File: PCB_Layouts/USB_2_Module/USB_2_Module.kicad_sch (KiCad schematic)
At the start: 3 parts, among them J1 USB_A, J2 Conn_01x10_Socket, J3 Conn_01x10_Socket

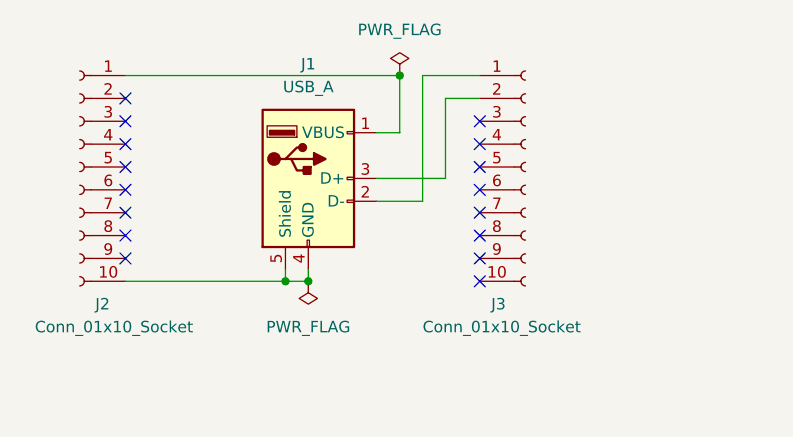
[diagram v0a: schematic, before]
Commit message: Adding USB 2 module and  quote
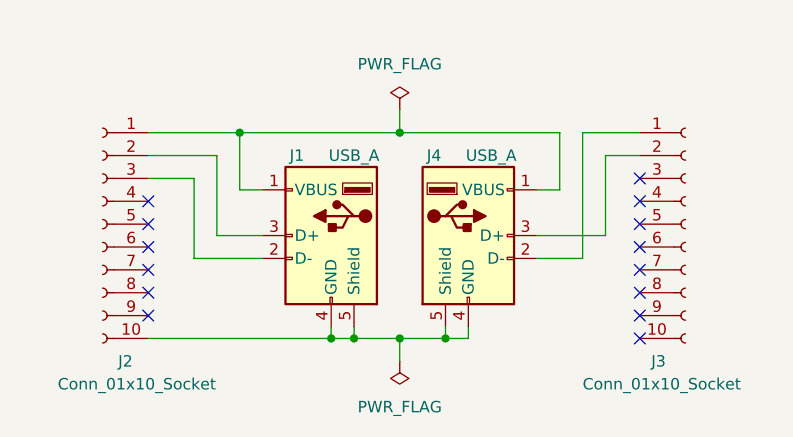
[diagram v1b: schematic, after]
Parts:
- added J4: USB_A, Connector_USB:USB_A_Stewart_SS-52100-001_Horizontal, symbol Connector:USB_A
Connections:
- net at J1.1 (VBUS), J2.1 (Pin_1): now also J4.1 (VBUS)
- net at J1.2 (D-): now also J2.3 (Pin_3); no longer J3.1 (Pin_1)
- net at J1.3 (D+): now also J2.2 (Pin_2); no longer J3.2 (Pin_2)
- net at J1.4 (GND), J1.5 (Shield), J2.10 (Pin_10): now also J4.4 (GND), J4.5 (Shield)
- new net: J3.1 (Pin_1), J4.2 (D-)
- new net: J3.2 (Pin_2), J4.3 (D+)
- no-connect marks 16 -> 14
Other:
- title: USB Interface for Bitcraze Crazyflie 2.0 -> USB 2 Interface for Bitcraze Crazyflie 2.0
